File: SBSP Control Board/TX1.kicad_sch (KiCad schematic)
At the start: 13 parts, among them U2 ADAR1000ACCZN

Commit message: 'finished' the first IC routing
need to re do and see what connections we need to make for programming. also need to see about better ground connections to the IC.
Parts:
- C15, C16, C17, C18, C19, C20, C21, C22, C47, C48, C49: footprint Capacitor_SMD:C_1206_3216Metric -> Resistor_SMD:R_0603_1608Metric
- R1: footprint Resistor_SMD:R_1206_3216Metric -> Resistor_SMD:R_0603_1608Metric
- U2: footprint CC-88-1_ADI -> adar1000:CC-88-1_ADI
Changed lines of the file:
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@@
 			)
 		)
-		(property "Footprint" "CC-88-1_ADI"
+		(property "Footprint" "adar1000:CC-88-1_ADI"
 			(at 133.35 147.32 0)
 			(hide yes)
@@
 			)
 		)
-		(property "Footprint" "Capacitor_SMD:C_1206_3216Metric"
+		(property "Footprint" "Resistor_SMD:R_0603_1608Metric"
 			(at 154.6352 186.69 0)
 			(hide yes)
@@
 			)
 		)
-		(property "Footprint" "Capacitor_SMD:C_1206_3216Metric"
+		(property "Footprint" "Resistor_SMD:R_0603_1608Metric"
 			(at 87.9602 160.02 0)
 			(hide yes)
@@
 			)
 		)
-		(property "Footprint" "Capacitor_SMD:C_1206_3216Metric"
+		(property "Footprint" "Resistor_SMD:R_0603_1608Metric"
 			(at 181.3052 186.69 0)
 			(hide yes)
@@
 			)
 		)
-		(property "Footprint" "Capacitor_SMD:C_1206_3216Metric"
+		(property "Footprint" "Resistor_SMD:R_0603_1608Metric"
 			(at 115.2652 186.69 0)
 			(hide yes)
@@
 			)
 		)
-		(property "Footprint" "Capacitor_SMD:C_1206_3216Metric"
+		(property "Footprint" "Resistor_SMD:R_0603_1608Metric"
 			(at 167.3352 186.69 0)
 			(hide yes)
@@
 			)
 		)
-		(property "Footprint" "CC-88-1_ADI"
+		(property "Footprint" "adar1000:CC-88-1_ADI"
 			(at 146.05 246.38 0)
 			(hide yes)
@@
 			)
 		)
-		(property "Footprint" "Capacitor_SMD:C_1206_3216Metric"
+		(property "Footprint" "Resistor_SMD:R_0603_1608Metric"
 			(at 141.9352 186.69 0)
 			(hide yes)
@@
 			)
 		)
-		(property "Footprint" "Capacitor_SMD:C_1206_3216Metric"
+		(property "Footprint" "Resistor_SMD:R_0603_1608Metric"
 			(at 76.5302 160.02 0)
 			(hide yes)
@@
 			)
 		)
-		(property "Footprint" "Capacitor_SMD:C_1206_3216Metric"
+		(property "Footprint" "Resistor_SMD:R_0603_1608Metric"
 			(at 99.3902 160.02 0)
 			(hide yes)
@@
 			)
 		)
-		(property "Footprint" "Resistor_SMD:R_1206_3216Metric"
+		(property "Footprint" "Resistor_SMD:R_0603_1608Metric"
 			(at 115.57 97.028 90)
 			(hide yes)
@@
 			)
 		)
-		(property "Footprint" "CC-88-1_ADI"
+		(property "Footprint" "adar1000:CC-88-1_ADI"
 			(at 124.46 64.77 0)
 			(hide yes)
@@
 			)
 		)
-		(property "Footprint" "Capacitor_SMD:C_1206_3216Metric"
+		(property "Footprint" "Resistor_SMD:R_0603_1608Metric"
 			(at 129.2352 186.69 0)
 			(hide yes)
@@
 			)
 		)
-		(property "Footprint" "Capacitor_SMD:C_1206_3216Metric"
+		(property "Footprint" "Resistor_SMD:R_0603_1608Metric"
 			(at 194.0052 186.69 0)
 			(hide yes)
@@
 			)
 		)
-		(property "Footprint" "Capacitor_SMD:C_1206_3216Metric"
+		(property "Footprint" "Resistor_SMD:R_0603_1608Metric"
 			(at 102.5652 186.69 0)
 			(hide yes)

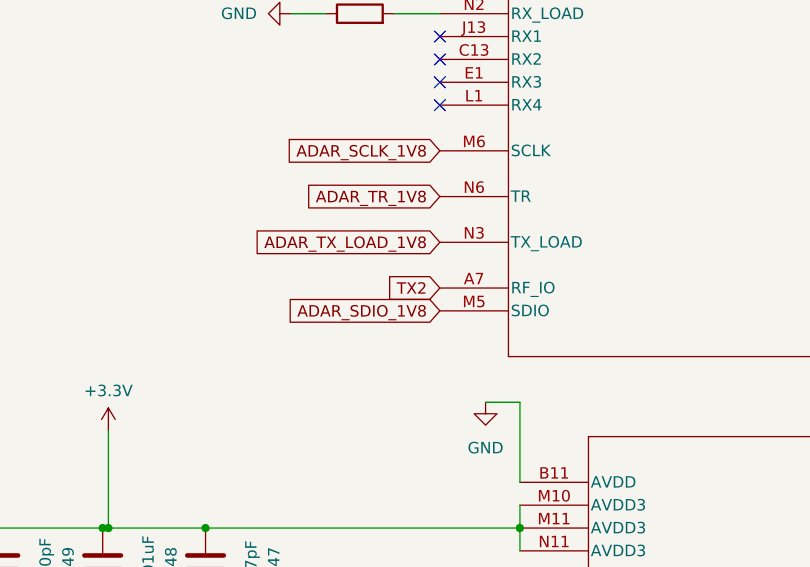
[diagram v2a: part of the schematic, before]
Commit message: finished implementing level shifting
just need to go look and do a run through to make sure it's all okay. also need to look into the power requirements for the +3/-5/-3 and make sure the nets are all correct. just double check the pdf with what we have wired.
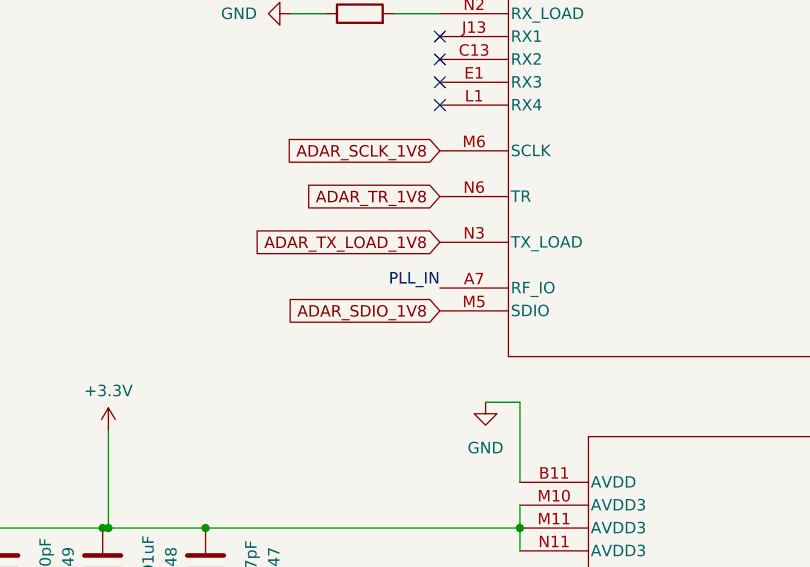
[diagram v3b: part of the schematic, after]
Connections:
- net TX2 renamed PLL_IN
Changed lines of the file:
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@@
+		)
+	)
+	(label "PLL_IN"
+		(at 124.46 125.73 180)
+		(effects
+			(font
+				(size 1.27 1.27)
+			)
+			(justify right bottom)
 		)
 	)
@@
 			)
 		)
-	)
-	(global_label "TX2"
-		(shape input)
-		(at 124.46 125.73 180)
-		(fields_autoplaced yes)
-		(effects
-			(font
-				(size 1.27 1.27)
-			)
-			(justify right)
-		)
-		(property "Intersheetrefs" "${INTERSHEET_REFS}"
-			(at 118.0882 125.73 0)
-			(hide yes)
-			(show_name no)
-			(do_not_autoplace no)
-			(effects
-				(font
-					(size 1.27 1.27)
-				)
-				(justify right)
-			)
-		)
